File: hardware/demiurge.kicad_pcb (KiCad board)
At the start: 2 copper layers, 40.1 x 109.9 mm, 135 parts, among them J2 PGM, U1 TL072, U2 TL072, U3 TL072, U4 TL072, U5 AMS1117-3.3, U6 74LVC1T45W6, U7 CH32V307RCT6, U8 TL072, U9 TL072, Y1 25MHz

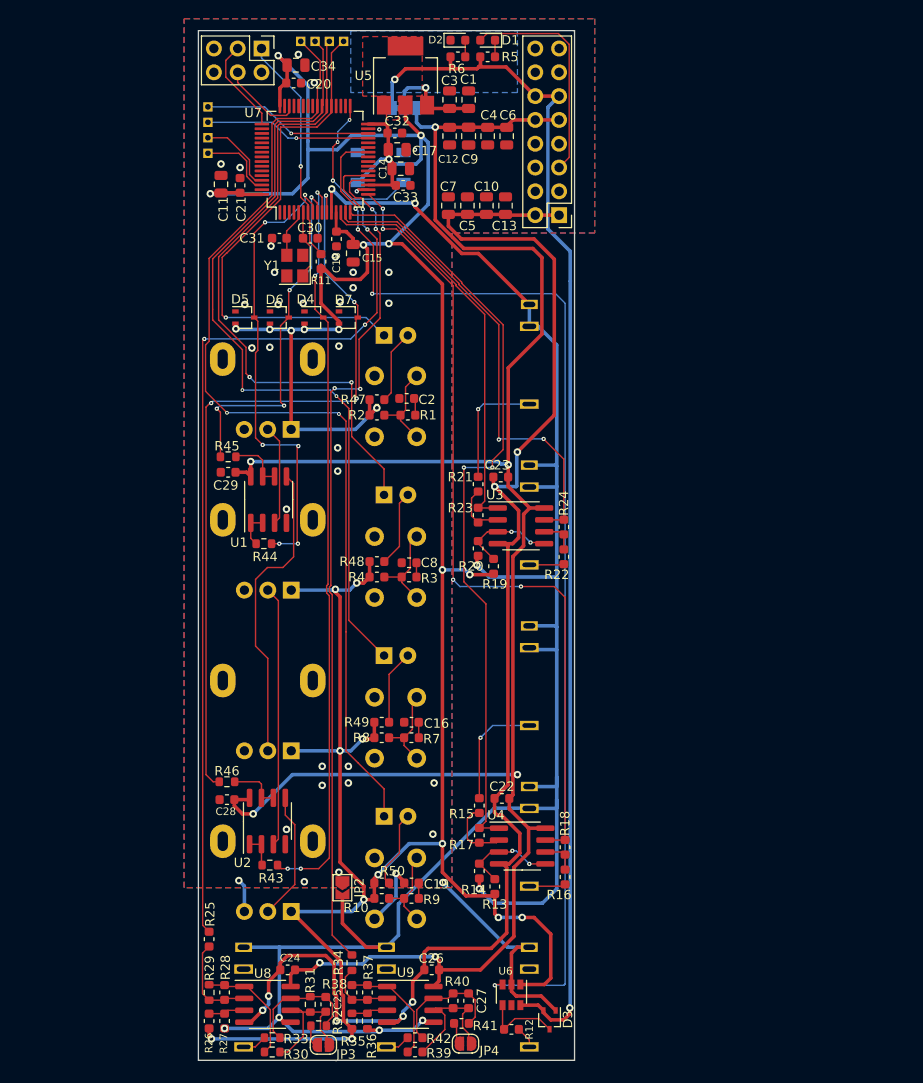
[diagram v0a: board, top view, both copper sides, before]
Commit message: First cut of the software. Not changed to RISC-V yet.
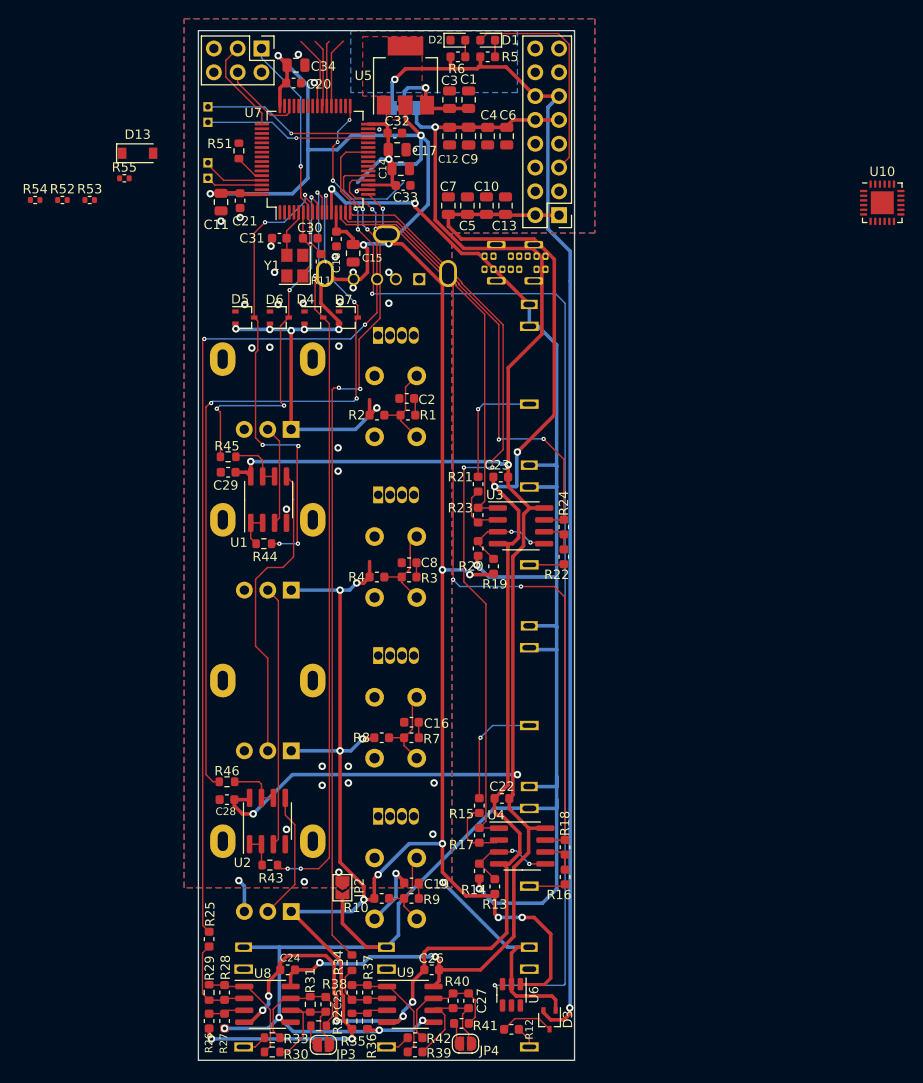
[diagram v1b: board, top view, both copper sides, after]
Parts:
- removed D12: WS2812B, LED_SMD:LED_WS2812B_PLCC4_5.0x5.0mm_P3.2mm
- removed R47, R48, R49, R50: 470, Resistor_SMD:R_0603_1608Metric
- removed TP5, TP6, TP7, TP8: ~, aaa:TestPoint_THTPad_1.0x1.0mm_Drill0.6mm
- added D13: ~, Diode_SMD:D_SOD-123, F.Cu at (70.0, 63.9)
- added J10: USB_C_Receptacle_USB2.0, aaa:USB_C_Receptacle_Vertical, B.Cu at (110.2, 75.6)
- added J11: USB_A, Connector_USB:USB_A_Molex_105057_Vertical, B.Cu at (100.0, 77.3)
- added R51: 10k, Resistor_SMD:R_0603_1608Metric, F.Cu at (80.8, 63.6)
- added R52: 5.1k, Resistor_SMD:R_0402_1005Metric, F.Cu at (61.9, 68.9)
- added R53: 5.1k, Resistor_SMD:R_0402_1005Metric, F.Cu at (64.9, 68.9)
- added R54: 22R, Resistor_SMD:R_0402_1005Metric, F.Cu at (59.0, 68.9)
- added R55: 22R, Resistor_SMD:R_0402_1005Metric, F.Cu at (68.6, 66.6)
- added U10: AW9523BTQR, Package_DFN_QFN:VQFN-24-1EP_4x4mm_P0.5mm_EP2.45x2.45mm, F.Cu at (149.4, 69.2)
- C31: value 12pF -> 20pF
- D10, D11, D8, D9: footprint LED_THT:LED_D3.0mm -> LED_THT:LED_D5.0mm-4_RGB
- R26, R35: value 68k -> 36k
- R27, R36: value 24k -> 22k
- U6: value 74LVC1T45W6 -> 74LVC1T45FZ4-7
- Y1: value 25MHz -> 16MHz
- moved TP1 2.67 mm to (77.5, 64.9)
- moved TP2 2.67 mm to (77.5, 66.5)
- moved C11 1.90 mm to (78.9, 69.1), turned to -90 degrees
- moved C21 1.63 mm to (80.9, 68.9), turned to -90 degrees
- moved D8 0.64 mm to (95.6, 83.3)
- moved D11 0.64 mm to (95.6, 134.6)
- moved D10 0.62 mm to (95.6, 117.5)
- moved D9 0.62 mm to (95.6, 100.3)
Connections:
- D10 pad 1: LED3 -> L2_R
- D10 pad 2: Net-(D10-Pad2) -> +3V3
- D11 pad 1: LED4 -> L3_R
- D11 pad 2: Net-(D11-Pad2) -> +3V3
- D8 pad 1: LED1 -> L0_R
- D8 pad 2: Net-(D8-Pad2) -> +3V3
- D9 pad 1: LED2 -> L1_R
- D9 pad 2: Net-(D9-Pad2) -> +3V3
- J2 pad 6: unconnected-(J2-Pad6) -> SWO
- TP2 pad 1: Net-(U7-Pad62) -> Net-(TP2-Pad1)
- U7 pad 27: unconnected-(U7-Pad27) -> DIR0
- U7 pad 29: Net-(TP3-Pad1) -> /Pot+LED/SCL
- U7 pad 30: Net-(TP4-Pad1) -> /Pot+LED/SDA
- U7 pad 33: RGB -> unconnected-(U7-Pad33)
- U7 pad 34: unconnected-(U7-Pad34) -> /Pot+LED/GPRST
- U7 pad 35: unconnected-(U7-Pad35) -> /Pot+LED/GPINT
- U7 pad 37: LED1 -> unconnected-(U7-Pad37)
- U7 pad 38: LED2 -> unconnected-(U7-Pad38)
- U7 pad 39: LED3 -> unconnected-(U7-Pad39)
- U7 pad 40: LED4 -> unconnected-(U7-Pad40)
- U7 pad 44: unconnected-(U7-Pad44) -> USB1_DM
- U7 pad 45: unconnected-(U7-Pad45) -> USB1_DP
- U7 pad 51: unconnected-(U7-Pad51) -> Net-(TP1-Pad1)
- U7 pad 52: unconnected-(U7-Pad52) -> Net-(TP2-Pad1)
- U7 pad 53: unconnected-(U7-Pad53) -> Net-(TP3-Pad1)
- U7 pad 54: unconnected-(U7-Pad54) -> Net-(TP4-Pad1)
- U7 pad 55: unconnected-(U7-Pad55) -> SWO
- U7 pad 58: unconnected-(U7-Pad58) -> USB2_DM
- U7 pad 59: unconnected-(U7-Pad59) -> USB2_DP
- U7 pad 61: Net-(TP1-Pad1) -> unconnected-(U7-Pad61)
- U7 pad 62: Net-(U7-Pad62) -> unconnected-(U7-Pad62)
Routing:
- net -12V: track 157.4 -> 0.00 mm, vias 7 -> 0
- net +12V: track 217.7 -> 375.1 mm, vias 7 -> 14
- net LED4: track 105.6 -> 0.00 mm, vias 2 -> 0
- net LED3: track 86.0 -> 0.00 mm, vias 2 -> 0
- net LED2: track 68.9 -> 0.00 mm, vias 2 -> 0
- net LED1: track 55.1 -> 0.00 mm, vias 1 -> 0
- net unconnected-(U7-Pad33): track 0.00 -> 17.8 mm, vias 0 -> 3
- net RGB: track 17.8 -> 0.00 mm, vias 3 -> 0
- net Net-(D11-Pad2): track 8.28 -> 0.00 mm
- net Net-(D9-Pad2): track 8.15 -> 0.00 mm
- net Net-(U7-Pad62): track 8.12 -> 0.00 mm
- net Net-(D10-Pad2): track 7.94 -> 0.00 mm
- net Net-(D8-Pad2): track 7.90 -> 0.00 mm
- net unconnected-(U7-Pad40): track 0.00 -> 7.88 mm
- net unconnected-(U7-Pad37): track 0.00 -> 7.48 mm
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
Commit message: Rev E updated to Rev F (WIP)
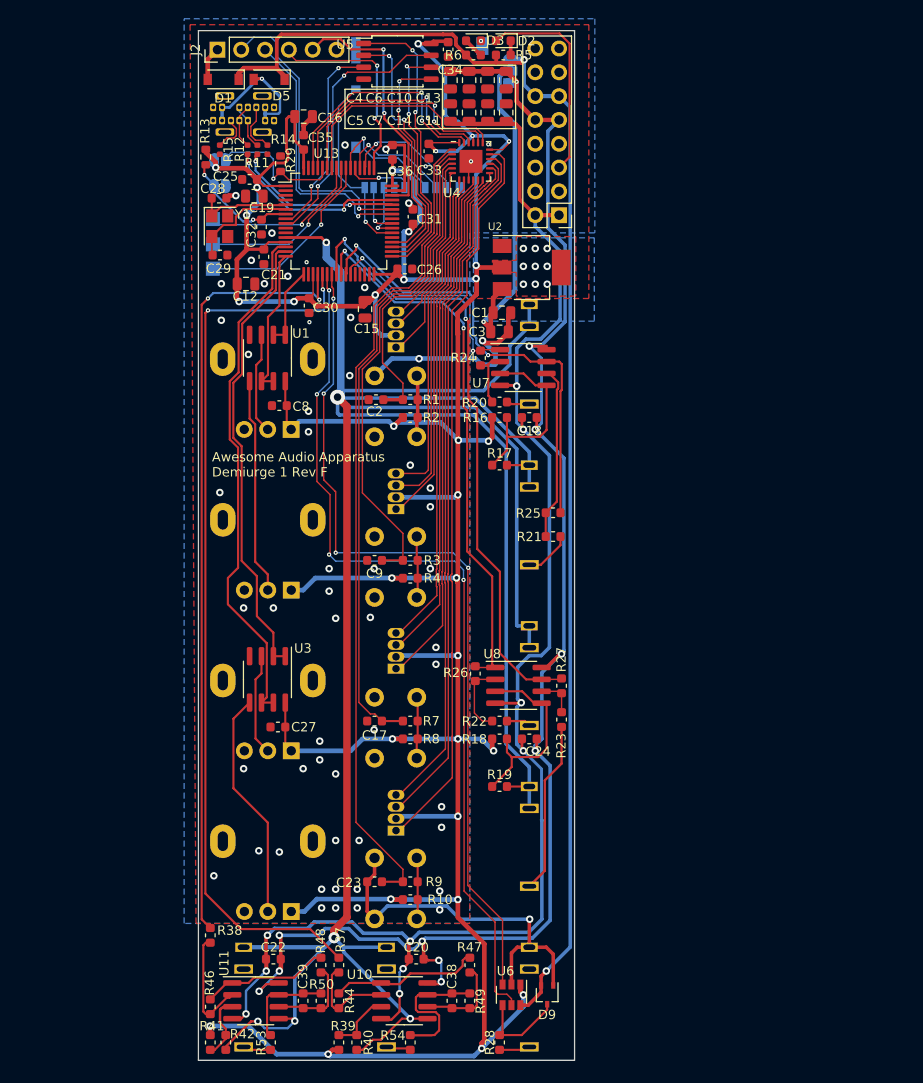
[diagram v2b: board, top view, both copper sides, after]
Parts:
- removed D4, D6, D7: BAT54SW, Package_TO_SOT_SMD:SOT-323_SC-70
- removed D8: ~, LED_THT:LED_D5.0mm-4_RGB
- removed J10: USB_C_Receptacle_USB2.0, aaa:USB_C_Receptacle_Vertical
- removed JP4: ~, Jumper:SolderJumper-2_P1.3mm_Open_RoundedPad1.0x1.5mm
- removed R30, R51: 10k, Resistor_SMD:R_0603_1608Metric
- removed R31, R32: 20k, Resistor_SMD:R_0603_1608Metric
- removed R33, R43, R45: 100, Resistor_SMD:R_0603_1608Metric
- removed R34: 1k, Resistor_SMD:R_0603_1608Metric
- removed R35: 36k, Resistor_SMD:R_0603_1608Metric
- removed R36: 22k, Resistor_SMD:R_0603_1608Metric
- removed R52: 5.1k, Resistor_SMD:R_0402_1005Metric
- removed R55: 22R, Resistor_SMD:R_0402_1005Metric
- removed TP4: ~, aaa:TestPoint_THTPad_1.0x1.0mm_Drill0.6mm
- removed U9: TL072, Package_SO:SOIC-8_3.9x4.9mm_P1.27mm
- added C35: 100nF, Capacitor_SMD:C_0603_1608Metric, F.Cu at (87.7, 62.7)
- added C36: 100nF, Capacitor_SMD:C_0603_1608Metric, F.Cu at (97.2, 63.8)
- added C38: 1nF, Capacitor_SMD:C_0603_1608Metric, F.Cu at (103.5, 154.3)
- added C39: 1nF, Capacitor_SMD:C_0603_1608Metric, F.Cu at (87.6, 154.3)
- added D12: ~, LED_THT:LED_D5.0mm-4_RGB, B.Cu at (97.5, 118.9)
- added J12: Micro_SD_Card_Det_Hirose_DM3AT, Connector_Card:microSD_HC_Hirose_DM3AT-SF-PEJM5, B.Cu at (100.1, 59.8)
- added R47: 10k, Resistor_SMD:R_0603_1608Metric, F.Cu at (105.4, 150.5)
- added R48: 10k, Resistor_SMD:R_0603_1608Metric, F.Cu at (89.5, 150.5)
- added R49: 20k, Resistor_SMD:R_0603_1608Metric, F.Cu at (105.4, 154.3)
- added R50: 20k, Resistor_SMD:R_0603_1608Metric, F.Cu at (89.5, 154.3)
- added U11: TL072, Package_SO:SOIC-8_3.9x4.9mm_P1.27mm, F.Cu at (82.5, 154.3)
- added U13: CH32V307RCT6, Package_QFP:LQFP-64_10x10mm_P0.5mm, F.Cu at (91.4, 71.1)
- C16, C19: value 100nF -> 22uF; footprint Capacitor_SMD:C_0603_1608Metric -> Capacitor_SMD:C_0805_2012Metric
- C17, C34, C9: value 22uF -> 100nF; footprint Capacitor_SMD:C_0805_2012Metric -> Capacitor_SMD:C_0603_1608Metric
- C25, C27: value 1nF -> 100nF
- C28, C29: value 100nF -> 20pF
- C30: value 12pF -> 100nF
- C31: value 20pF -> 100nF
- D1: value Red -> ~; footprint LED_SMD:LED_0603_1608Metric -> Diode_SMD:D_SOD-123
- D13: footprint Diode_SMD:D_SOD-123 -> LED_THT:LED_D5.0mm-4_RGB; moved to B.Cu
- D2: value Green -> Red
- D3: value BAT54SW -> Green; footprint Package_TO_SOT_SMD:SOT-323_SC-70 -> LED_SMD:LED_0603_1608Metric
- D5: value BAT54SW -> ~; footprint Package_TO_SOT_SMD:SOT-323_SC-70 -> Diode_SMD:D_SOD-123
- D9: value ~ -> BAT54SW; footprint LED_THT:LED_D5.0mm-4_RGB -> Package_TO_SOT_SMD:SOT-323_SC-70; moved to F.Cu
- J11: value USB_A -> ~; footprint Connector_USB:USB_A_Molex_105057_Vertical -> aaa:USB_C_Receptacle_Vertical
- J2: value PGM -> Conn_01x06; footprint Connector_PinHeader_2.54mm:PinHeader_2x03_P2.54mm_Vertical -> Connector_PinHeader_2.54mm:PinHeader_1x06_P2.54mm_Vertical
- JP1: footprint Jumper:SolderJumper-3_P1.3mm_Bridged12_Pad1.0x1.5mm -> Jumper:SolderJumper-3_P1.3mm_Bridged12_RoundedPad1.0x1.5mm
- JP2: value SolderJumper_2_Open -> ~; footprint Jumper:SolderJumper-2_P1.3mm_Open_TrianglePad1.0x1.5mm -> Jumper:SolderJumper-2_P1.3mm_Open_RoundedPad1.0x1.5mm; moved to B.Cu
- JP3: moved to B.Cu
- R11: value 10k -> 22R; footprint Resistor_SMD:R_0603_1608Metric -> Resistor_SMD:R_0402_1005Metric
- R12: value 1k -> 22R; footprint Resistor_SMD:R_0603_1608Metric -> Resistor_SMD:R_0402_1005Metric
- R13: value 18k -> 10k
- R14: value 13k -> 5.1k; footprint Resistor_SMD:R_0603_1608Metric -> Resistor_SMD:R_0402_1005Metric
- R15: value 20k -> 5.1k; footprint Resistor_SMD:R_0603_1608Metric -> Resistor_SMD:R_0402_1005Metric
- R16: value 20k -> 18k
- R17: value 3k3 -> 13k
- R18: value 3k3 -> 18k
- R19: value 18k -> 13k
- R20: value 13k -> 20k
- R23: value 3k3 -> 20k
- R25: value 1k -> 3k3
- R26: value 36k -> 3k3
- R27: value 22k -> 3k3
- R28: value 10k -> 1k
- R39: value 10k -> 36k
- R40: value 20k -> 22k
- R41: value 20k -> 36k
- R42: value 100 -> 22k
- R44, R46: value 100 -> 33k
- R53: value 5.1k -> 100; footprint Resistor_SMD:R_0402_1005Metric -> Resistor_SMD:R_0603_1608Metric
- R54: value 22R -> 100; footprint Resistor_SMD:R_0402_1005Metric -> Resistor_SMD:R_0603_1608Metric
- TP1: value ~ -> TP1; footprint aaa:TestPoint_THTPad_1.0x1.0mm_Drill0.6mm -> TestPoint:TestPoint_Pad_1.5x1.5mm
- TP2: value ~ -> TP2; footprint aaa:TestPoint_THTPad_1.0x1.0mm_Drill0.6mm -> TestPoint:TestPoint_Pad_1.5x1.5mm
- TP3: value ~ -> SWO; footprint aaa:TestPoint_THTPad_1.0x1.0mm_Drill0.6mm -> TestPoint:TestPoint_Pad_1.5x1.5mm
- U1, U3: value TL072 -> MCP6002
- U10: value AW9523BTQR -> TL072; footprint Package_DFN_QFN:VQFN-24-1EP_4x4mm_P0.5mm_EP2.45x2.45mm -> Package_SO:SOIC-8_3.9x4.9mm_P1.27mm
- U2: value TL072 -> AMS1117-3.3; footprint Package_SO:SOIC-8_3.9x4.9mm_P1.27mm -> Package_TO_SOT_SMD:SOT-223-3_TabPin2
- U4: value TL072 -> AW9523BTQR; footprint Package_SO:SOIC-8_3.9x4.9mm_P1.27mm -> Package_DFN_QFN:VQFN-24-1EP_4x4mm_P0.5mm_EP2.45x2.45mm
- U5: value AMS1117-3.3 -> W25Q128JVS; footprint Package_TO_SOT_SMD:SOT-223-3_TabPin2 -> Package_SO:SOIC-8_5.23x5.23mm_P1.27mm
- U6: value 74LVC1T45FZ4-7 -> 74LVC1T45W6
- U7: value CH32V307RCT6 -> TL072; footprint Package_QFP:LQFP-64_10x10mm_P0.5mm -> Package_SO:SOIC-8_3.9x4.9mm_P1.27mm
- moved D3 104.8 mm to (105.8, 51.9), turned to 180 degrees
- moved U10 99.2 mm to (98.4, 154.3)
- moved R54 98.4 mm to (99.1, 158.8), turned to 90 degrees
- moved R12 98.0 mm to (81.7, 63.5), turned to -90 degrees
- moved C20 94.4 mm to (99.7, 149.9), turned to 180 degrees
- moved JP3 92.3 mm to (78.7, 67.4)
- moved R53 91.9 mm to (84.2, 158.8), turned to 90 degrees
- moved R29 88.7 mm to (85.2, 65.0)
- moved C25 88.4 mm to (81.9, 66.7), turned to 180 degrees
- moved R13 83.7 mm to (77.2, 64.3), turned to 90 degrees
- moved R14 80.2 mm to (83.8, 63.5), turned to -90 degrees
- moved JP2 78.7 mm to (78.7, 64.6), turned to 180 degrees
- moved D13 77.3 mm to (97.5, 136.1), turned to 90 degrees
- moved R15 75.3 mm to (78.7, 63.5), turned to -90 degrees
- moved C19 75.2 mm to (82.4, 68.5)
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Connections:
- net Net-(R45-Pad1) renamed AD6
- C1 pad 1: /VIN -> Net-(C1-Pad1)
- C10 pad 1: GND -> +12V
- C10 pad 2: -12V -> GND
- C11 pad 1: +3V3 -> GND
- C11 pad 2: GND -> -12V
- C12 pad 1: +12V -> +3V3
- C13 pad 1: GND -> +12V
- C13 pad 2: -12V -> GND
- C14 pad 1: +3V3 -> GND
- C14 pad 2: GND -> -12V
- C16 pad 1: B2 -> +3V3
- C17 pad 1: +3V3 -> B2
- C18 pad 1: +3V3 -> +12V
- C18 pad 2: GND -> -12V
- C19 pad 1: B3 -> +3V3
- C20 pad 1: +3V3 -> +12V
- C20 pad 2: GND -> -12V
- C23 pad 1: +12V -> B3
- C23 pad 2: -12V -> GND
- C25 pad 1: Net-(C25-Pad1) -> +3V3
- C25 pad 2: Net-(C25-Pad2) -> GND
- C26 pad 1: +12V -> +3V3
- C26 pad 2: -12V -> GND
- C27 pad 1: Net-(C27-Pad1) -> +3V3
- C27 pad 2: Net-(C27-Pad2) -> GND
- C28 pad 1: +12V -> Net-(C28-Pad1)
- C29 pad 1: +12V -> Net-(C29-Pad1)
- C3 pad 1: /VIN -> Net-(C1-Pad1)
- C30 pad 1: Net-(C30-Pad1) -> +3V3
- C31 pad 1: Net-(C31-Pad1) -> +3V3
- C32 pad 1: +3V3 -> NRST
- C8 pad 1: B1 -> +3V3
- C9 pad 1: +12V -> B1
- D1 pad 1: Net-(D1-Pad1) -> +5V
- D1 pad 2: Net-(D1-Pad2) -> Net-(J2-Pad1)
- D10 pad 1: L2_R -> L0_R
- D10 pad 3: L2_G -> L0_G
- D10 pad 4: L2_B -> L0_B
- D11 pad 1: L3_R -> L1_R
- D11 pad 3: L3_G -> L1_G
- D11 pad 4: L3_B -> L1_B
- D13 pad 1: +5V -> L3_R
- D13 pad 2: VBUS -> +3V3
- D2 pad 1: GND -> Net-(D2-Pad1)
- D3 pad 2: +5V -> Net-(D3-Pad2)
- D5 pad 1: GND -> +5V
- D5 pad 2: +3V3 -> VBUS
- D9 pad 1: L1_R -> GND
- D9 pad 2: +3V3 -> +5V
- D9 pad 3: L1_G -> Net-(D9-Pad3)
- J1 pad 5: Net-(D1-Pad2) -> Net-(D2-Pad2)
- J2 pad 1: EN -> Net-(J2-Pad1)
- J2 pad 2: unconnected-(J2-Pad2) -> USART1_RX
- J2 pad 3: SWCLK -> USART1_TX
- J2 pad 4: SWDIO -> SWCLK
- J2 pad 5: GND -> SWDIO
- J2 pad 6: SWO -> GND
- JP1 pad 2: /VIN -> Net-(C1-Pad1)
- JP2 pad 1: GND -> BOOT0
- JP2 pad 2: GNDA -> +3V3
- JP3 pad 1: Net-(C25-Pad1) -> GND
- JP3 pad 2: Net-(JP3-Pad2) -> NRST
- R11 pad 1: +3V3 -> Net-(J11-PadA7)
- R11 pad 2: EN -> DM
- R12 pad 1: Net-(J7-PadT) -> Net-(J11-PadA6)
- R12 pad 2: Net-(D3-Pad3) -> DP
- R13 pad 1: Net-(R13-Pad1) -> NRST
- R14 pad 1: GNDA -> Net-(J11-PadB5)
- R14 pad 2: Net-(R13-Pad1) -> GND
- R15 pad 1: Net-(R15-Pad1) -> Net-(J11-PadA5)
- R15 pad 2: Net-(J5-PadT) -> GND
- R16 pad 2: Net-(J6-PadT) -> +3V3
- R17 pad 1: /Analog-In2/Input1 -> GNDA
- R17 pad 2: Net-(R15-Pad1) -> Net-(R16-Pad1)
- R18 pad 1: /Analog-In2/Input2 -> Net-(R18-Pad1)
- R18 pad 2: Net-(R16-Pad1) -> +3V3
- R19 pad 1: Net-(R19-Pad1) -> GNDA
- R19 pad 2: +3V3 -> Net-(R18-Pad1)
- R20 pad 1: GNDA -> Net-(R20-Pad1)
- R20 pad 2: Net-(R19-Pad1) -> Net-(J3-PadT)
- R21 pad 2: Net-(J3-PadT) -> Net-(J4-PadT)
- R22 pad 2: Net-(J4-PadT) -> Net-(J5-PadT)
- R23 pad 1: /Analog-In1/Input1 -> Net-(R23-Pad1)
- R23 pad 2: Net-(R21-Pad1) -> Net-(J6-PadT)
- R24 pad 1: /Analog-In1/Input2 -> AD3
- R24 pad 2: Net-(R22-Pad1) -> Net-(R20-Pad1)
- R25 pad 1: Net-(R25-Pad1) -> AD2
- R25 pad 2: DAC2 -> Net-(R21-Pad1)
- R26 pad 1: +3V3 -> AD1
- R26 pad 2: Net-(U8-Pad3) -> Net-(R22-Pad1)
- R27 pad 1: Net-(U8-Pad3) -> AD0
- R27 pad 2: GNDA -> Net-(R23-Pad1)
- R28 pad 1: Net-(R28-Pad1) -> Net-(J7-PadT)
- R28 pad 2: Net-(R25-Pad1) -> Net-(D9-Pad3)
- R29 pad 1: Net-(R28-Pad1) -> GND
- R29 pad 2: Net-(R25-Pad1) -> BOOT0
- R37 pad 1: Net-(R37-Pad1) -> Net-(R44-Pad2)
- R37 pad 2: Net-(R34-Pad1) -> AO0
- R38 pad 1: Net-(R37-Pad1) -> Net-(R46-Pad2)
- R38 pad 2: Net-(R34-Pad1) -> AO1
- R39 pad 1: Net-(C27-Pad1) -> +3V3
- R39 pad 2: Net-(R37-Pad1) -> Net-(R39-Pad2)
- R40 pad 1: Net-(C27-Pad2) -> Net-(R39-Pad2)
- R40 pad 2: Net-(C27-Pad1) -> GNDA
- R41 pad 1: Net-(C27-Pad2) -> +3V3
- R41 pad 2: Net-(JP4-Pad2) -> Net-(R41-Pad2)
- R42 pad 1: Net-(J9-PadT) -> Net-(R41-Pad2)
- R42 pad 2: Net-(C27-Pad2) -> GNDA
- R44 pad 1: Net-(R44-Pad1) -> Net-(R47-Pad2)
- R44 pad 2: POT1 -> Net-(R44-Pad2)
- R46 pad 2: POT4 -> Net-(R46-Pad2)
- R5 pad 2: Net-(D1-Pad1) -> Net-(D2-Pad1)
- R53 pad 1: Net-(J10-PadB5) -> Net-(J8-PadT)
- R53 pad 2: GND -> Net-(C39-Pad2)
- R54 pad 1: Net-(J10-PadA7) -> Net-(J9-PadT)
- R54 pad 2: USB1_DM -> Net-(C38-Pad2)
- R6 pad 2: Net-(D2-Pad2) -> Net-(D3-Pad2)
- TP1 pad 1: Net-(TP1-Pad1) -> TP1
- TP2 pad 1: Net-(TP2-Pad1) -> TP2
- TP3 pad 1: Net-(TP3-Pad1) -> TP3
- U1 pad 1: Net-(R44-Pad1) -> AD7
- U1 pad 2: Net-(R44-Pad1) -> AD7
- U1 pad 5: Net-(RV3-Pad2) -> Net-(RV2-Pad2)
- U1 pad 8: +12V -> +3V3
- U10 pad 1: B3 -> Net-(R47-Pad2)
- U10 pad 2: B2 -> Net-(R44-Pad2)
- U10 pad 3: B1 -> Net-(R39-Pad2)
- U10 pad 4: B0 -> -12V
- U10 pad 5: L0_B -> GNDA
- U10 pad 6: L0_G -> Net-(C38-Pad1)
- U10 pad 7: L0_R -> Net-(C38-Pad2)
- U10 pad 8: L1_B -> +12V
- U2 pad 1: Net-(R43-Pad1) -> GND
- U2 pad 2: Net-(R43-Pad1) -> +3V3
- U2 pad 3: Net-(RV2-Pad2) -> Net-(C1-Pad1)
- U3 pad 1: /Analog-In1/Input1 -> AD5
- U3 pad 2: Net-(R21-Pad1) -> AD5
- U3 pad 3: Net-(R19-Pad1) -> Net-(RV3-Pad2)
- U3 pad 4: -12V -> GND
- U3 pad 5: Net-(R19-Pad1) -> Net-(RV4-Pad2)
- U3 pad 6: Net-(R22-Pad1) -> AD4
- U3 pad 7: /Analog-In1/Input2 -> AD4
- U3 pad 8: +12V -> +3V3
- U4 pad 1: /Analog-In2/Input1 -> B3
- U4 pad 2: Net-(R15-Pad1) -> B2
- U4 pad 3: Net-(R13-Pad1) -> B1
- U4 pad 4: -12V -> B0
- U4 pad 5: Net-(R13-Pad1) -> L0_B
- U4 pad 6: Net-(R16-Pad1) -> L0_G
- U4 pad 7: /Analog-In2/Input2 -> L0_R
- U4 pad 8: +12V -> L1_B
- U5 pad 1: GND -> FLASH_CS
- U5 pad 2: +3V3 -> FLASH_MISO
- U5 pad 3: /VIN -> ~{FLASH_WP}
- U6 pad 4: Net-(D3-Pad3) -> Net-(D9-Pad3)
- U7 pad 1: unconnected-(U7-Pad1) -> AD3
- U7 pad 2: unconnected-(U7-Pad2) -> Net-(R20-Pad1)
- U7 pad 3: unconnected-(U7-Pad3) -> Net-(R16-Pad1)
- U7 pad 4: unconnected-(U7-Pad4) -> -12V
- U7 pad 5: Net-(C31-Pad1) -> Net-(R16-Pad1)
- U7 pad 6: Net-(C30-Pad1) -> Net-(R21-Pad1)
- U7 pad 7: EN -> AD2
- U7 pad 8: POT1 -> +12V
- U8 pad 1: Net-(R28-Pad1) -> AD1
- U8 pad 2: Net-(R25-Pad1) -> Net-(R22-Pad1)
- U8 pad 3: Net-(U8-Pad3) -> Net-(R18-Pad1)
- U8 pad 5: GNDA -> Net-(R18-Pad1)
- U8 pad 6: Net-(C25-Pad1) -> Net-(R23-Pad1)
- U8 pad 7: Net-(C25-Pad2) -> AD0
- Y1 pad 1: Net-(C30-Pad1) -> Net-(C28-Pad1)
- Y1 pad 2: GND -> Net-(C29-Pad1)
- Y1 pad 3: Net-(C31-Pad1) -> (no net)
- Y1 pad 4: GND -> (no net)
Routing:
- net +12V: track 375.1 -> 165.5 mm, vias 14 -> 11
- net -12V: track 0.00 -> 166.0 mm, vias 0 -> 10
- net DAC2: track 101.8 -> 0.00 mm, vias 4 -> 0
- net AO0: track 0.00 -> 95.7 mm, vias 0 -> 2
- net DIR0: track 0.00 -> 95.3 mm, vias 0 -> 4
- net DAC1: track 91.1 -> 0.00 mm, vias 4 -> 0
- net /Analog-In2/Input2: track 86.4 -> 0.00 mm, vias 4 -> 0
- net B3: track 1.66 -> 88.0 mm
- net GNDA: track 215.1 -> 301.2 mm, vias 8 -> 6
- net AO1: track 0.00 -> 83.0 mm, vias 0 -> 2
- net POT4: track 82.5 -> 0.00 mm, vias 4 -> 0
- net /Analog-In2/Input1: track 81.9 -> 0.00 mm, vias 2 -> 0
- net POT3: track 80.3 -> 0.00 mm, vias 4 -> 0
- net L3_R: track 0.00 -> 78.6 mm
- net L3_G: track 0.00 -> 74.9 mm
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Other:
- rule pad_to_mask_clearance: 0 -> 0.0508
- board text added: "Awesome Audio Apparatus Demiurge 1 Rev F"
- board text removed: "Awesome Audio Apparatus Demiurge aaa-k1 rev. 4"

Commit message: AW9523 is discontinued @ LCSC. Changing to AW20036, capable of up to 12 RGB LEDs.
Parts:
- added C37: 4.7uF, Capacitor_SMD:C_0805_2012Metric, F.Cu at (92.2, 81.6)
- added C40: 1uF, Capacitor_SMD:C_0603_1608Metric, F.Cu at (104.8, 63.2)
- added C41: 4.7uF, Capacitor_SMD:C_0805_2012Metric, F.Cu at (106.0, 71.9)
- added C42: 100nF, Capacitor_SMD:C_0603_1608Metric, F.Cu at (109.8, 64.5)
- added C43: 100nF, Capacitor_SMD:C_0603_1608Metric, F.Cu at (106.4, 63.2)
- added R30: 0R, Capacitor_SMD:C_0603_1608Metric, F.Cu at (98.2, 65.2)
- added R31: 0R, Capacitor_SMD:C_0603_1608Metric, F.Cu at (93.3, 78.8)
- added R32: 51R, Resistor_SMD:R_0603_1608Metric, F.Cu at (100.8, 74.7)
- added R33: 20R, Resistor_SMD:R_0603_1608Metric, F.Cu at (101.0, 77.8)
- added R34: 20R, Resistor_SMD:R_0603_1608Metric, F.Cu at (102.4, 74.7)
- added R35: 51R, Resistor_SMD:R_0603_1608Metric, F.Cu at (102.7, 77.8)
- added R36: 20R, Resistor_SMD:R_0603_1608Metric, F.Cu at (104.0, 74.7)
- added R43: 20R, Resistor_SMD:R_0603_1608Metric, F.Cu at (104.3, 77.8)
- U4: value AW9523BTQR -> AW20036; footprint Package_DFN_QFN:VQFN-24-1EP_4x4mm_P0.5mm_EP2.45x2.45mm -> Package_DFN_QFN:QFN-32-1EP_4x4mm_P0.4mm_EP2.65x2.65mm_ThermalVias
- moved U4 2.89 mm to (106.4, 67.5)
- moved C15 1.08 mm to (94.2, 81.6)
- moved C35 0.88 mm to (86.8, 62.7)
- moved C36 0.45 mm to (96.7, 63.8)
- moved R29 0.08 mm to (85.3, 65.0)
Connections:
- D10 pad 1: L0_R -> LED_R1
- D10 pad 2: +3V3 -> LED_C1
- D10 pad 3: L0_G -> LED_G1
- D10 pad 4: L0_B -> LED_B1
- D11 pad 1: L1_R -> LED_R1
- D11 pad 2: +3V3 -> LED_C2
- D11 pad 3: L1_G -> LED_G1
- D11 pad 4: L1_B -> LED_B1
- D12 pad 1: L2_R -> LED_R1
- D12 pad 2: +3V3 -> LED_C3
- D12 pad 3: L2_G -> LED_G1
- D12 pad 4: L2_B -> LED_B1
- D13 pad 1: L3_R -> LED_R2
- D13 pad 2: +3V3 -> LED_C1
- D13 pad 3: L3_G -> LED_G2
- D13 pad 4: L3_B -> LED_B2
- U13 pad 10: unconnected-(U13-Pad10) -> AD0
- U13 pad 11: unconnected-(U13-Pad11) -> AD1
- U13 pad 24: AD0 -> AD2
- U13 pad 25: AD1 -> AD3
- U13 pad 26: AD2 -> B3
- U13 pad 27: AD3 -> B2
- U13 pad 28: unconnected-(U13-Pad28) -> B1
- U13 pad 29: unconnected-(U13-Pad29) -> B0
- U13 pad 30: unconnected-(U13-Pad30) -> Net-(U13-Pad30)
- U13 pad 31: GND -> Net-(U13-Pad31)
- U13 pad 47: GND -> Net-(R30-Pad1)
- U13 pad 62: GPRST -> HWEN
- U4 pad 1: B3 -> Net-(R32-Pad2)
- U4 pad 10: L1_G -> unconnected-(U4-Pad10)
- U4 pad 11: L1_R -> unconnected-(U4-Pad11)
- U4 pad 12: L2_B -> unconnected-(U4-Pad12)
- U4 pad 13: L2_G -> +3V3
- U4 pad 14: L2_R -> (no net)
- U4 pad 15: L3_B -> (no net)
- U4 pad 16: L3_G -> (no net)
- U4 pad 17: L3_R -> (no net)
- U4 pad 18: +3V3 -> (no net)
- U4 pad 19: SCL -> (no net)
- U4 pad 2: B2 -> Net-(R33-Pad2)
- U4 pad 20: SDA -> LED_C3
- U4 pad 21: +3V3 -> LED_C2
- U4 pad 22: GPINT -> LED_C1
- U4 pad 23: GPRST -> +3V3
- U4 pad 24: +3V3 -> GND
- U4 pad 3: B1 -> Net-(R34-Pad2)
- U4 pad 4: B0 -> Net-(R35-Pad2)
- U4 pad 5: L0_B -> Net-(R36-Pad2)
- U4 pad 6: L0_G -> Net-(R43-Pad2)
- U4 pad 7: L0_R -> unconnected-(U4-Pad7)
- U4 pad 8: L1_B -> unconnected-(U4-Pad8)
- U4 pad 9: GND -> unconnected-(U4-Pad9)
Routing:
- net LED_C1: track 0.00 -> 82.9 mm, vias 0 -> 2
- net L3_R: track 78.6 -> 0.00 mm
- net L3_G: track 74.9 -> 0.00 mm
- net L3_B: track 72.7 -> 0.00 mm
- net LED_G2: track 0.00 -> 63.8 mm, vias 0 -> 2
- net LED_R2: track 0.00 -> 61.1 mm
- net LED_C3: track 0.00 -> 59.5 mm, vias 0 -> 1
- net LED_B2: track 0.00 -> 59.4 mm, vias 0 -> 2
- net L2_R: track 58.6 -> 0.00 mm
- net L2_G: track 54.8 -> 0.00 mm
- net LED_R1: track 0.00 -> 53.2 mm
- net LED_B1: track 0.00 -> 52.7 mm, vias 0 -> 3
- net L2_B: track 52.4 -> 0.00 mm
- net LED_G1: track 0.00 -> 49.5 mm, vias 0 -> 3
- net LED_C2: track 0.00 -> 43.1 mm, vias 0 -> 1
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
